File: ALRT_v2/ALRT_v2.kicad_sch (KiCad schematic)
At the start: 37 parts, among them J1 Battery, J2 Electrodes, J3 Vibrator, J4 HR_PCB, Q1 2N7002, Q2 2N7002, Q3 MMBT3904, SW1 PTS810_SJM_250_SMTR_LFS, U1 Beetle_ESP32-C3_v2, U2 MPU-6050

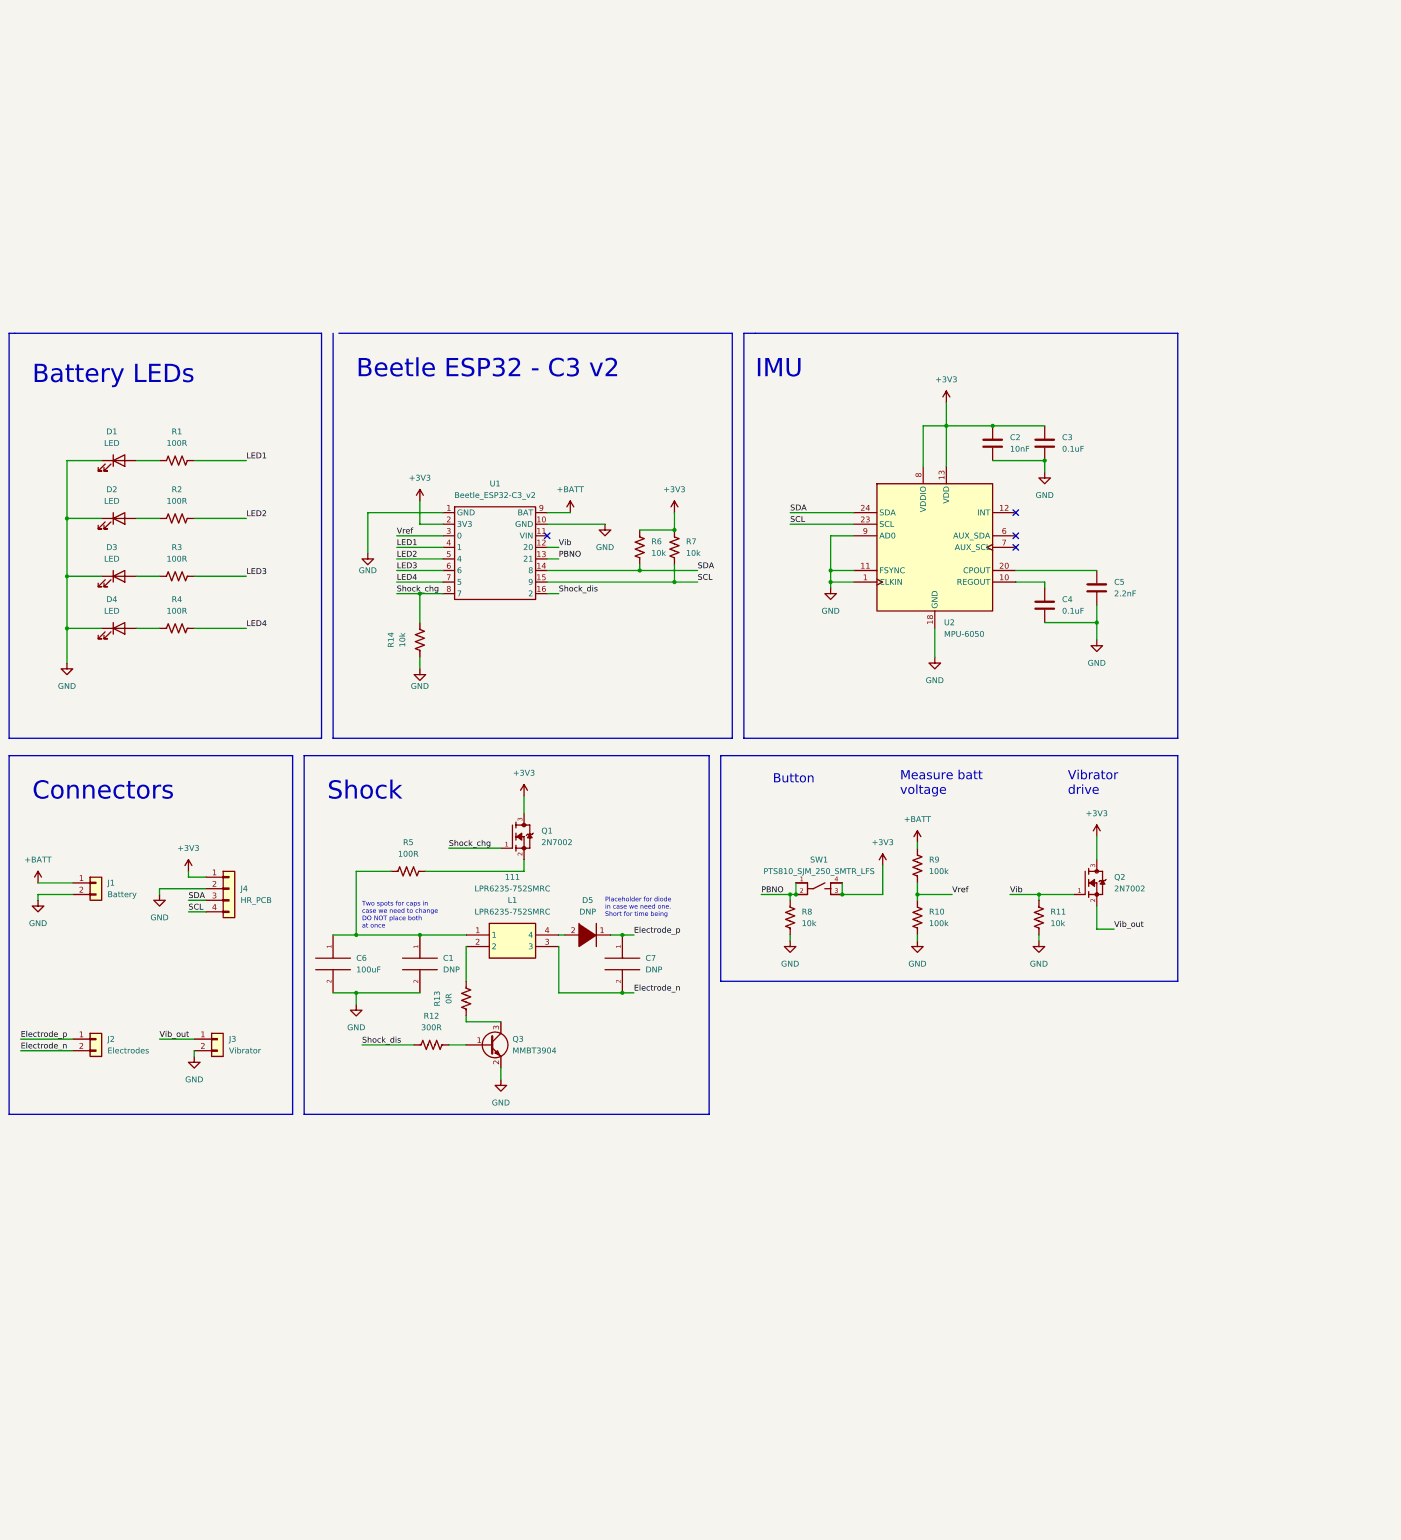
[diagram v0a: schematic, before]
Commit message: started removing beetle board and reconfigured charge circuit
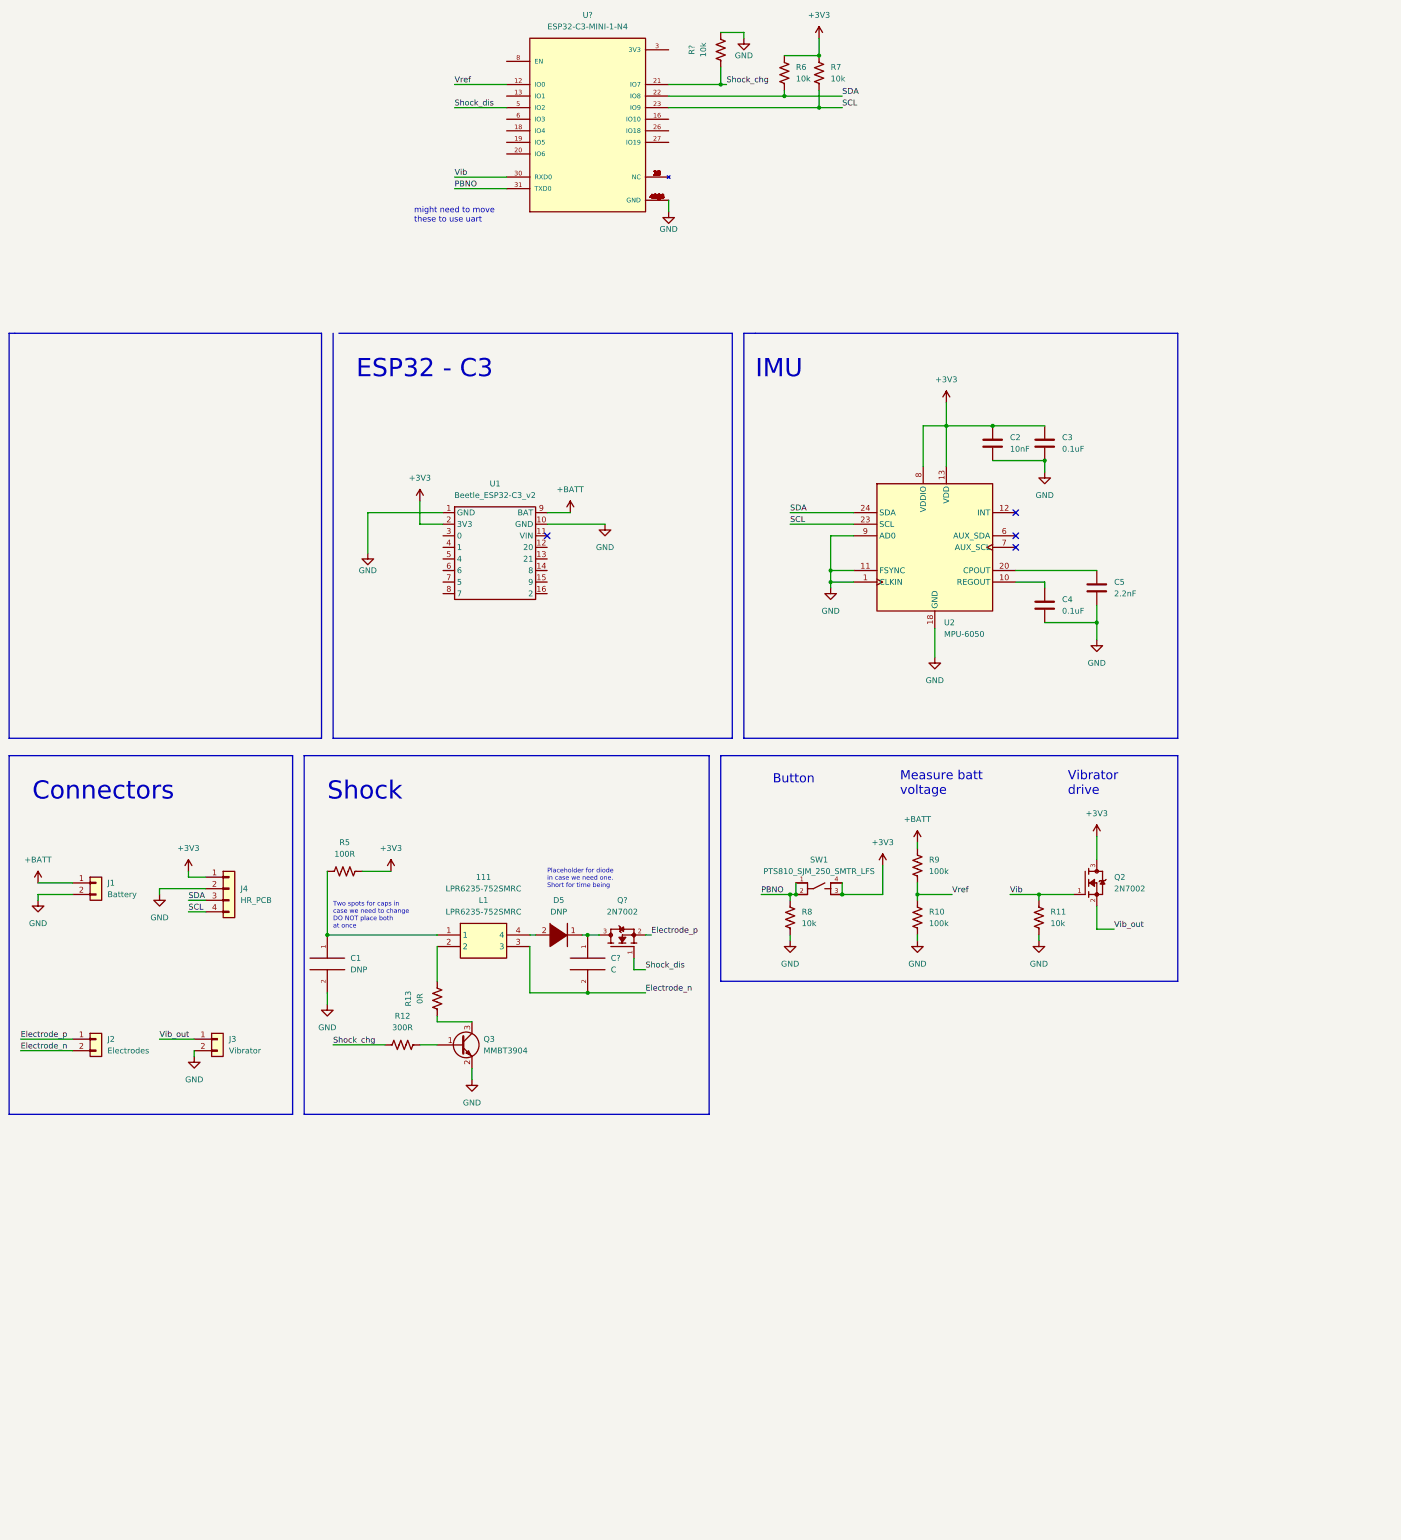
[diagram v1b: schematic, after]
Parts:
- removed C6: 100uF, Capacitor_SMD:C_1206_3216Metric, symbol pspice:C
- removed C7: DNP, Capacitor_SMD:C_0603_1608Metric, symbol pspice:C
- removed D1, D2, D3, D4: LED, LED_SMD:LED_0603_1608Metric, symbol Device:LED
- removed Q1: 2N7002, 2N7002:SOT95P240X111-3N, symbol 2N7002:2N7002
- removed R1, R2, R3, R4: 100R, Resistor_SMD:R_0603_1608Metric, symbol Device:R_US
- removed R14: 10k, Resistor_SMD:R_0603_1608Metric, symbol Device:R_US
- added C?: C, symbol pspice:C
- added Q?: 2N7002, 2N7002:SOT95P240X111-3N, symbol 2N7002:2N7002
- added R?: 10k, Resistor_SMD:R_0603_1608Metric, symbol Device:R_US
- added U?: ESP32-C3-MINI-1-N4, ESP32-C3-MINI-1-N4:XCVR_ESP32-C3-MINI-1-N4, symbol ESP32-C3-MINI-1-N4:ESP32-C3-MINI-1-N4
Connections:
- net +3V3: now also R5.1
- net Electrode_n: now also C?.2
- net Electrode_p: now also Q?.2; no longer D5.1 (A)
- net GND: now also R?.1, U?.1 (GND), U?.11 (GND), U?.14 (GND), U?.2 (GND), U?.36 (GND), U?.37 (GND), U?.38 (GND), U?.39 (GND), U?.40 (GND), U?.41 (GND), U?.42 (GND), U?.43 (GND), U?.44 (GND), U?.45 (GND), U?.46 (GND), U?.47 (GND), U?.48 (GND), U?.49_1 (GND), U?.49_2 (GND), U?.49_3 (GND), U?.49_4 (GND), U?.49_5 (GND), U?.49_6 (GND), U?.49_7 (GND), U?.49_8 (GND), U?.49_9 (GND), U?.50 (GND), U?.51 (GND), U?.52 (GND), U?.53 (GND)
- net PBNO: now also U?.31 (TXD0); no longer U1.13 (21)
- net SCL: now also U?.23 (IO9); no longer U1.15 (9)
- net SDA: now also U?.22 (IO8); no longer U1.14 (8)
- net Shock_chg: now also R12.2, R?.2, U?.21 (IO7); no longer U1.8 (7)
- net Shock_dis: now also Q?.1, U?.5 (IO2); no longer R12.2, U1.16 (2)
- net Vib: now also U?.30 (RXD0); no longer U1.12 (20)
- net Vref: now also U?.12 (IO0); no longer U1.3 (0)
- net LED1: no longer names the net of U1.4 (1)
- net LED2: no longer names the net of U1.5 (4)
- net LED3: no longer names the net of U1.6
- net LED4: no longer names the net of U1.7 (5)
- new net: C?.1, D5.1 (A), Q?.3
- new net: U?.10 (NC), U?.15 (NC), U?.17 (NC), U?.24 (NC), U?.25 (NC), U?.28 (NC), U?.29 (NC), U?.32 (NC), U?.33 (NC), U?.34 (NC), U?.35 (NC), U?.4 (NC), U?.7 (NC), U?.9 (NC)
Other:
- note added: "ESP32 - C3"
- note added: "might need to move these to use uart"
- note removed: "Battery LEDs"
- note removed: "Beetle ESP32 - C3 v2"
- moved on the sheet: 111, C1, D5, Q3, R12, R13, R5, R6, R7

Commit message: initial daughterboard removal
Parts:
- removed C1: DNP, Capacitor_SMD:C_0805_2012Metric, symbol pspice:C
- removed C?: C, symbol pspice:C
- removed U1: Beetle_ESP32-C3_v2, ALRT_v1:Beetle_ESP32_C3, symbol ALRT:Beetle_ESP32-C3_v2
- added C1: DNP, Capacitor_SMD:C_0603_1608Metric, symbol Device:C
- added C10: 1uF, Capacitor_SMD:C_0603_1608Metric, symbol Device:C
- added C11: ?uF, Capacitor_SMD:C_0603_1608Metric, symbol Device:C
- added C12, C8, C9: 10uF, Capacitor_SMD:C_0603_1608Metric, symbol Device:C
- added C13: 100nF, Capacitor_SMD:C_0603_1608Metric, symbol Device:C
- added C6, C7: 4.7uF, Capacitor_SMD:C_0603_1608Metric, symbol Device:C
- added D1: LED, LED_SMD:LED_0603_1608Metric, symbol Device:LED
- added D2, D3: DNP, Diode_SMD:D_SOD-123, symbol pspice:DIODE
- added J5: 2305018-2, CONN_2305018-2_TEC, symbol 2024-03-31_17-47-15:2305018-2
- added R1: 470R, Resistor_SMD:R_0603_1608Metric, symbol Device:R_US
- added R14: 200k, Resistor_SMD:R_0603_1608Metric, symbol Device:R_US
- added R15: 10k, Resistor_SMD:R_0603_1608Metric, symbol Device:R_US
- added R2: 2k, Resistor_SMD:R_0603_1608Metric, symbol Device:R_US
- added R3, R4: 5.1k, Resistor_SMD:R_0603_1608Metric, symbol Device:R_US
- added U3: MCP73831T-2ACI/OT, SOT-23-5_MC_MCH, symbol 2024-03-31_17-26-03:MCP73831T-2ACI_OT
- added U4: RT9080-33GJ5, TSOT-23-5_RIT, symbol 2024-03-31_18-03-44:RT9080-33GJ5
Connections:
- net +3V3: now also U?.3 (3V3), C12.1, C13.1, C9.1, R15.1, U4.5 (VOUT)
- net +BATT: now also C6.1, D2.2 (K), U3.3 (VBAT)
- net Electrode_n: now also C11.2
- net GND: now also C1.2, C10.2, C12.2, C13.2, C6.2, C7.2, C8.2, C9.2, J5.A1 (GND), J5.A12 (GND), J5.B1 (GND), J5.B12 (GND), R3.2, R4.2, U4.2 (GND)
- net at D5.1 (A), Q?.3: now also C11.1
- net at 111.1, R5.2: now also C1.1
- net D-: now reaches U?.26 (IO18)
- net D-: now also J5.A7 (D-), J5.B7 (D-)
- net D+: now reaches U?.27 (IO19)
- net D+: now also J5.A6 (D+), J5.B6 (D+)
- net at U?.8 (EN): now also C10.1, R15.2
- new net: C8.1, D2.1 (A), D3.1 (A), R14.1, U4.1 (VIN)
- new net: J5.B5 (CC2), R4.1
- new net: D1.1 (K), R1.1
- new net: R1.2, U3.1 (STAT)
- new net: R2.1, U3.2 (VSS)
- new net: R2.2, U3.5 (PROG)
- new net: R14.2, U4.3 (EN)
- new net: J5.A5 (CC1), R3.1
- new net +VUSB: C7.1, D1.2 (A), D3.2 (K), J5.A4 (VBUS), J5.A9 (VBUS), J5.B4 (VBUS), J5.B9 (VBUS), U3.4 (VDD)
- no-connect marks 4 -> 13
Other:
- note added: "3v3 LDO"
- note added: "Battery Charger"
- note added: "USB-C"
- moved on the sheet: C2, C3, C4, C5, R6, R7, R?, U2, U?
